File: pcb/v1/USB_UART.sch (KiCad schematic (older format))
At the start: 11 parts, among them J4 USB_B_Mini, J5 UART, U10 FT232RL

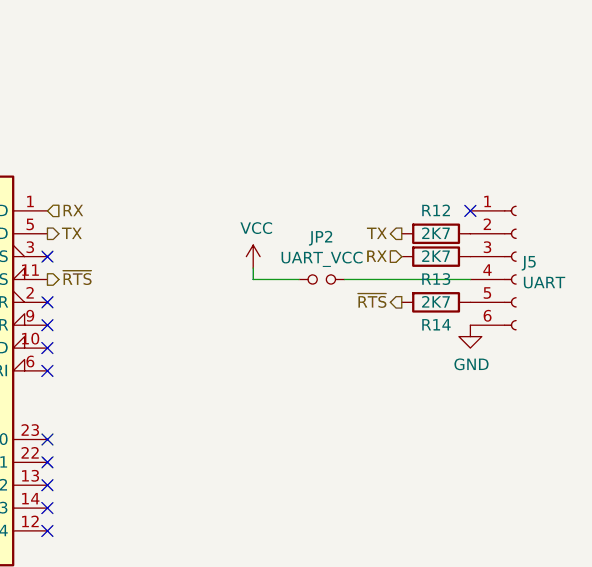
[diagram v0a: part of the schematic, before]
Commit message: Clean up routing
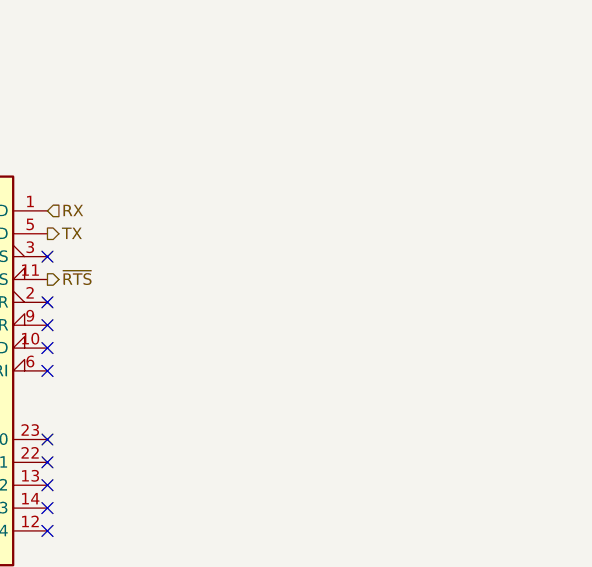
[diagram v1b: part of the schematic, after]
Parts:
- removed J5: UART, Connector_PinHeader_2.54mm:PinHeader_1x06_P2.54mm_Vertical, symbol Connector:Conn_01x06_Female
- removed JP2: UART_VCC, Connector_PinHeader_2.54mm:PinHeader_1x02_P2.54mm_Vertical, symbol Device:Jumper_NO_Small
- removed R12, R13, R14: 2K7, Resistor_THT:R_Axial_DIN0207_L6.3mm_D2.5mm_P10.16mm_Horizontal, symbol Device:R
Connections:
- no-connect marks 15 -> 14
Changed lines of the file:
@@
 Text Label 4200 3150 0    50   ~ 0
 USBD-
-$Comp
-L Connector:Conn_01x06_Female J5
-U 1 1 60B8677D
-P 9550 2950
-F 0 "J5" H 9578 2926 50  0000 L CNN
-F 1 "UART" H 9578 2835 50  0000 L CNN
-F 2 "Connector_PinHeader_2.54mm:PinHeader_1x06_P2.54mm_Vertical" H 9550 2950 50  0001 C CNN
-F 3 "~" H 9550 2950 50  0001 C CNN
-	1    9550 2950
-	1    0    0    -1
-$EndComp
-$Comp
-L Device:R R12
-U 1 1 60B8780A
-P 9200 2850
-F 0 "R12" V 9100 2850 50  0000 C CNN
-F 1 "2K7" V 9200 2850 50  0000 C CNN
-F 2 "Resistor_THT:R_Axial_DIN0207_L6.3mm_D2.5mm_P10.16mm_Horizontal" V 9130 2850 50  0001 C CNN
-F 3 "~" H 9200 2850 50  0001 C CNN
-	1    9200 2850
-	0    1    1    0
-$EndComp
-NoConn ~ 9350 2750
-$Comp
-L Device:R R13
-U 1 1 60B8845F
-P 9200 2950
-F 0 "R13" V 9300 2950 50  0000 C CNN
-F 1 "2K7" V 9200 2950 50  0000 C CNN
-F 2 "Resistor_THT:R_Axial_DIN0207_L6.3mm_D2.5mm_P10.16mm_Horizontal" V 9130 2950 50  0001 C CNN
-F 3 "~" H 9200 2950 50  0001 C CNN
-	1    9200 2950
-	0    1    1    0
-$EndComp
-Text HLabel 9050 2950 0    50   Input ~ 0
-RX
-Text HLabel 9050 2850 0    50   Output ~ 0
-TX
-$Comp
-L Device:Jumper_NO_Small JP2
-U 1 1 60B88B00
-P 8700 3050
-F 0 "JP2" H 8700 3235 50  0000 C CNN
-F 1 "UART_VCC" H 8700 3144 50  0000 C CNN
-F 2 "Connector_PinHeader_2.54mm:PinHeader_1x02_P2.54mm_Vertical" H 8700 3050 50  0001 C CNN
-F 3 "~" H 8700 3050 50  0001 C CNN
-	1    8700 3050
-	1    0    0    -1
-$EndComp
-Wire Wire Line
-	8800 3050 9350 3050
-$Comp
-L power:VCC #PWR049
-U 1 1 60B8B1B0
-P 8400 3000
-F 0 "#PWR049" H 8400 2850 50  0001 C CNN
-F 1 "VCC" H 8415 3173 50  0000 C CNN
-F 2 "" H 8400 3000 50  0001 C CNN
-F 3 "" H 8400 3000 50  0001 C CNN
-	1    8400 3000
-	1    0    0    -1
-$EndComp
-Wire Wire Line
-	8400 3000 8400 3050
-Wire Wire Line
-	8400 3050 8600 3050
-$Comp
-L Device:R R14
-U 1 1 60B8BFD6
-P 9200 3150
-F 0 "R14" V 9300 3150 50  0000 C CNN
-F 1 "2K7" V 9200 3150 50  0000 C CNN
-F 2 "Resistor_THT:R_Axial_DIN0207_L6.3mm_D2.5mm_P10.16mm_Horizontal" V 9130 3150 50  0001 C CNN
-F 3 "~" H 9200 3150 50  0001 C CNN
-	1    9200 3150
-	0    1    1    0
-$EndComp
-Text HLabel 9050 3150 0    50   Output ~ 0
-~RTS
-$Comp
-L power:GND #PWR068
-U 1 1 60B8C642
-P 9350 3250
-F 0 "#PWR068" H 9350 3000 50  0001 C CNN
-F 1 "GND" H 9355 3077 50  0000 C CNN
-F 2 "" H 9350 3250 50  0001 C CNN
-F 3 "" H 9350 3250 50  0001 C CNN
-	1    9350 3250
-	1    0    0    -1
-$EndComp
 $EndSCHEMATC
